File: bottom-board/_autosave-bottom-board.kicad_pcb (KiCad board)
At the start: 2 copper layers, 184 x 94 mm, 156 parts, among them P1 USB_B, P10 JACK_TRS_6PINS, P11 JACK_TRS_6PINS, P12 JACK_TRS_6PINS, P13 JACK_TRS_6PINS, P14 RJ45, P2 USB_A, P3 AudioJack3, P4 AS0A823-H4SB-7H, P5 BARREL_JACK, P6 AudioJack3, P7 AudioJack3, P8 HMI_DATA, P9 SERIAL_DEBUG, Q1 J110, Q12 2N7002, Q13 2N7002, Q2 J110, U1 TS2596, U10 RT9742MNGJ5, U11 6N137S, U12 ISL83491, U13 AP2120N-3.3, U2 LD1117S50TR_SOT223, U3 CODECODER-WM8731SEDS_V(SSOP28), U4 AT24CS08-STUM, U5 TS5A3159ADBVR

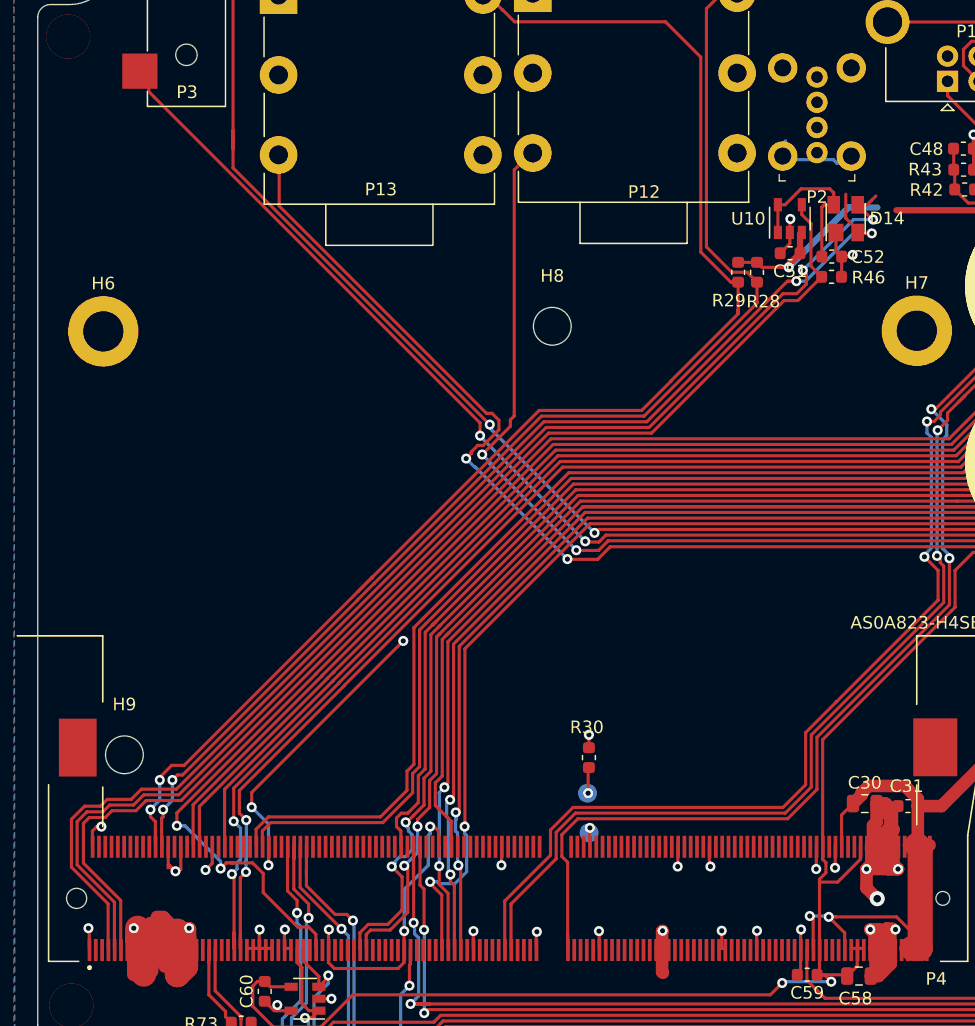
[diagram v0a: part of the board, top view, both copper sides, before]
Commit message: reposistioned screw holes
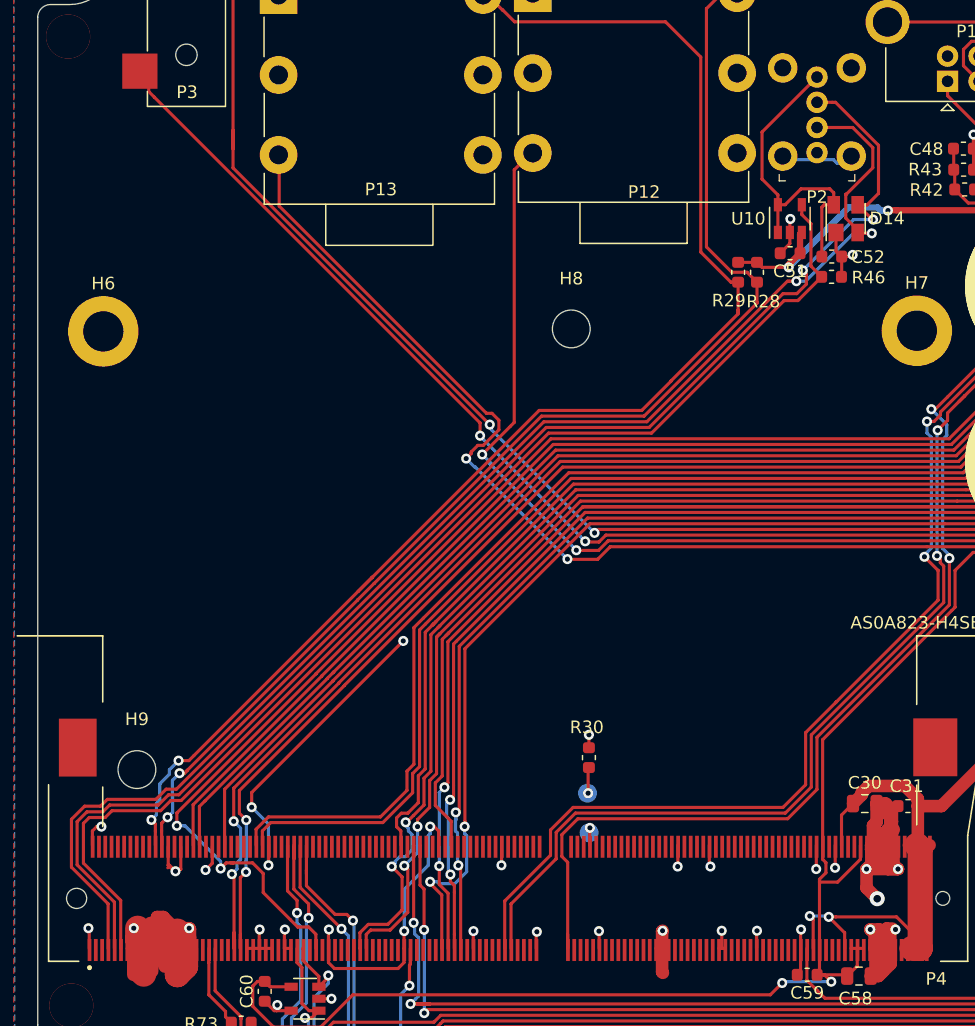
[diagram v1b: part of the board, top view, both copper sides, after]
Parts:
- moved H9 1.54 mm to (71.2, 107.5)
- moved H8 1.52 mm to (105.8, 72.5)
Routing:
- net Net-(C52-Pad2): track 13.4 -> 25.9 mm
- net USB_HOST_DM: track 98.9 -> 109.4 mm
- net USB_HOST_DP: track 98.9 -> 108.6 mm
- net +5V: track 258.5 -> 260.1 mm, vias 9 -> 10
- net OUT1_DETECT: track 96.8 -> 97.7 mm
